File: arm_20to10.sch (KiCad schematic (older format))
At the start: 10 parts, among them J1 ARM_20PIN, J2 ARM_10PIN, SW1 DUAL_SWITCH_INV, U1 AAT3221 or LP5907

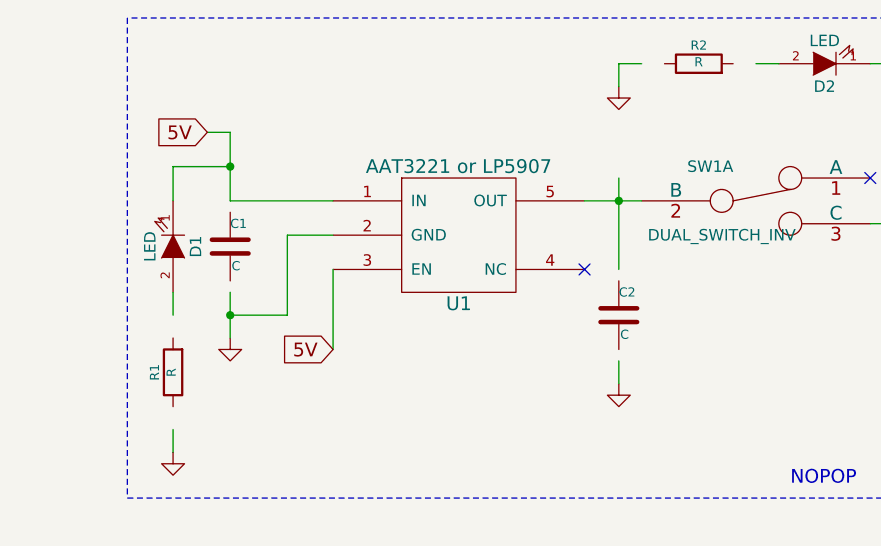
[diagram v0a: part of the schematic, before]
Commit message: - set some comp values
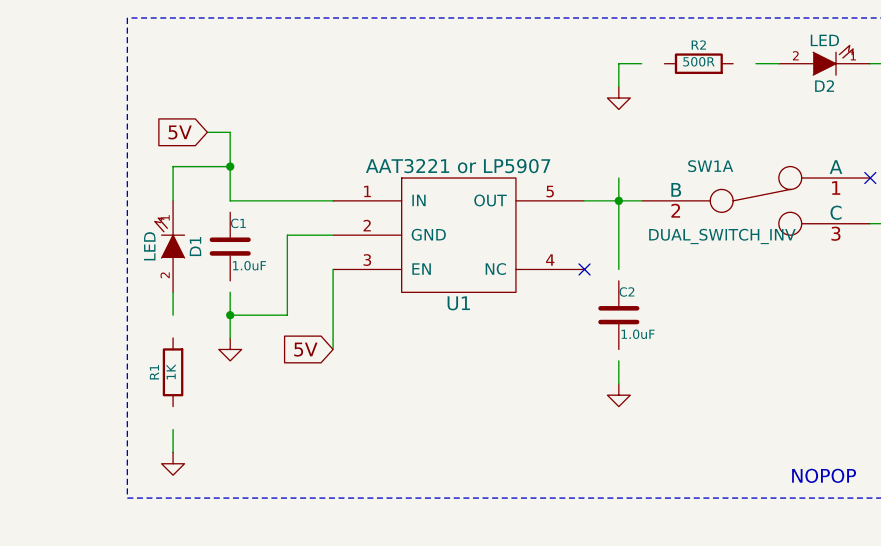
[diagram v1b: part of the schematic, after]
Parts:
- C1, C2: value C -> 1.0uF
- R1: value R -> 1K
- R2: value R -> 500R
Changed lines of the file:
@@
 P 8550 2200
 F 0 "C2" H 8550 2300 40  0000 L CNN
-F 1 "C" H 8556 2115 40  0000 L CNN
+F 1 "1.0uF" H 8556 2115 40  0000 L CNN
 F 2 "~" H 8588 2050 30  0000 C CNN
 F 3 "~" H 8550 2200 60  0000 C CNN
@@
 $EndComp
 NoConn ~ 8400 2000
-$Comp
-L C C1
-U 1 1 52FC308F
-P 6850 1900
-F 0 "C1" H 6850 2000 40  0000 L CNN
-F 1 "C" H 6856 1815 40  0000 L CNN
-F 2 "~" H 6888 1750 30  0000 C CNN
-F 3 "~" H 6850 1900 60  0000 C CNN
-	1    6850 1900
-	1    0    0    -1
-$EndComp
 Text GLabel 6750 1400 0    60   Input ~ 0
 5V
@@
 P 8900 1100
 F 0 "R2" V 8980 1100 40  0000 C CNN
-F 1 "R" V 8907 1101 40  0000 C CNN
+F 1 "500R" V 8907 1101 40  0000 C CNN
 F 2 "~" V 8830 1100 30  0000 C CNN
 F 3 "~" H 8900 1100 30  0000 C CNN
@@
 P 6600 2450
 F 0 "R1" V 6680 2450 40  0000 C CNN
-F 1 "R" V 6607 2451 40  0000 C CNN
+F 1 "1K" V 6607 2451 40  0000 C CNN
 F 2 "~" V 6530 2450 30  0000 C CNN
 F 3 "~" H 6600 2450 30  0000 C CNN
@@
 	9850 1100 9850 1800
 Connection ~ 9850 1800
+$Comp
+L C C1
+U 1 1 531B43FC
+P 6850 1900
+F 0 "C1" H 6850 2000 40  0000 L CNN
+F 1 "1.0uF" H 6856 1815 40  0000 L CNN
+F 2 "~" H 6888 1750 30  0000 C CNN
+F 3 "~" H 6850 1900 60  0000 C CNN
+	1    6850 1900
+	1    0    0    -1
+$EndComp
 $EndSCHEMATC

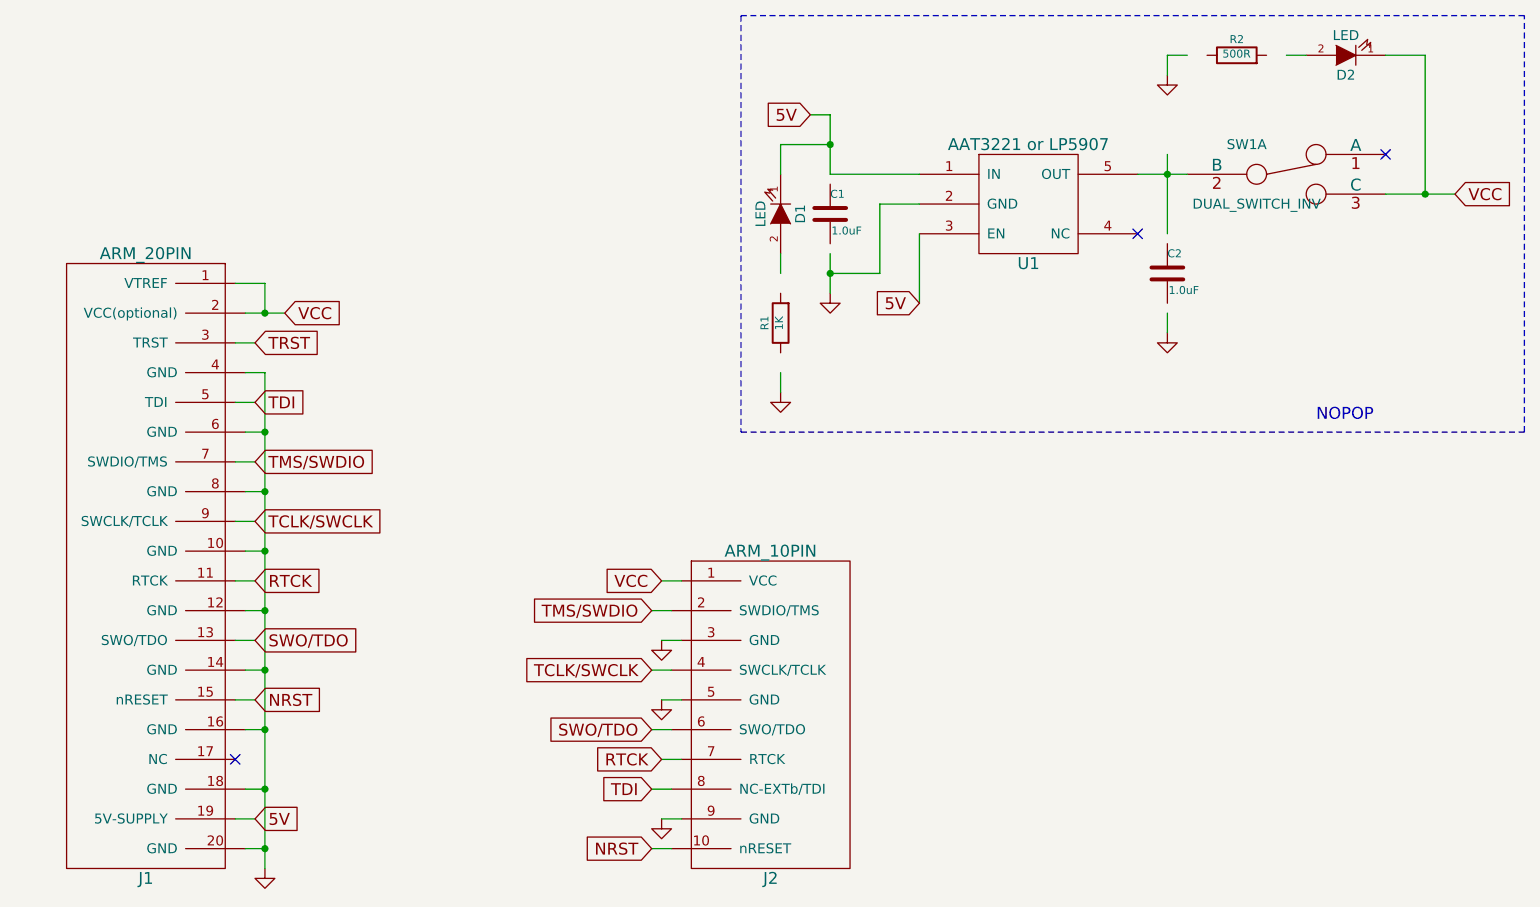
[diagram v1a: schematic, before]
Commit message: - redo with 0402 resistors
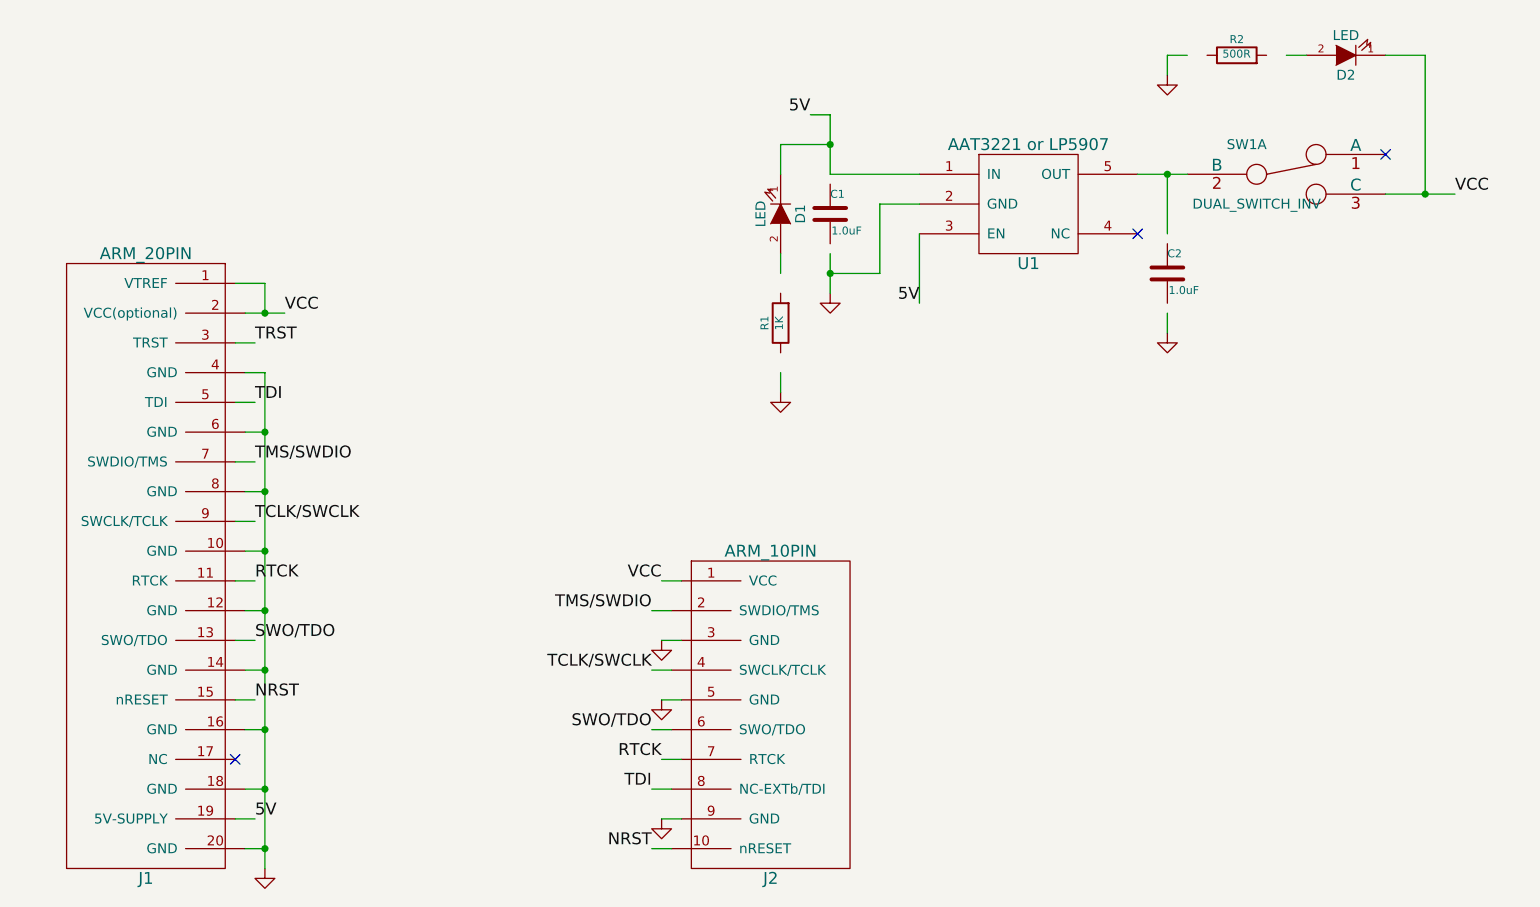
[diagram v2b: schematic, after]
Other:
- note removed: "NOPOP"
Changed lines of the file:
@@
 Sheet 1 1
 Title ""
-Date "8 mar 2014"
+Date "23 apr 2014"
 Rev ""
 Comp ""
@@
 	1    0    0    -1
 $EndComp
-Text GLabel 3950 3150 2    60   Input ~ 0
-TMS/SWDIO
-Text GLabel 3950 4050 2    60   Input ~ 0
-SWO/TDO
-Text GLabel 3950 4350 2    60   Input ~ 0
-NRST
 Wire Wire Line
 	3950 3150 3850 3150
@@
 Wire Wire Line
 	3950 4350 3850 4350
-Text GLabel 3950 2850 2    60   Input ~ 0
-TDI
 Wire Wire Line
 	3950 2850 3850 2850
-Text GLabel 3950 2550 2    60   Input ~ 0
-TRST
 Wire Wire Line
 	3950 2550 3850 2550
@@
 Wire Wire Line
 	6000 4650 6100 4650
-Text GLabel 5950 5100 0    60   Input ~ 0
-NRST
 Wire Wire Line
 	5950 5100 6050 5100
@@
 Wire Wire Line
 	6100 4050 6000 4050
-Text GLabel 5950 3900 0    60   Input ~ 0
-TMS/SWDIO
 Wire Wire Line
 	5950 3900 6050 3900
 Wire Wire Line
 	5950 4200 6050 4200
-Text GLabel 5950 4500 0    60   Input ~ 0
-SWO/TDO
 Wire Wire Line
 	6050 4500 5950 4500
-Text GLabel 5950 4800 0    60   Input ~ 0
-TDI
 Wire Wire Line
 	5950 4800 6050 4800
-Text GLabel 3950 4950 2    60   Input ~ 0
-5V
 Wire Wire Line
 	3950 4950 3850 4950
-Text GLabel 6000 3750 0    60   Input ~ 0
-VCC
 Wire Wire Line
 	6100 3750 6000 3750
-Text GLabel 4100 2400 2    60   Input ~ 0
-VCC
 Wire Wire Line
 	3900 2400 4100 2400
@@
 Connection ~ 4000 2400
 NoConn ~ 3850 4650
-Text GLabel 3950 3750 2    60   Input ~ 0
-RTCK
-Text GLabel 6000 4650 0    60   Input ~ 0
-RTCK
 $Comp
 L GND #PWR03
@@
 	1    0    0    -1
 $EndComp
-Text GLabel 3950 3450 2    60   Input ~ 0
-TCLK/SWCLK
-Text GLabel 5950 4200 0    60   Input ~ 0
-TCLK/SWCLK
 $Comp
 L GND #PWR04
@@
 $EndComp
 NoConn ~ 8400 2000
-Text GLabel 6750 1400 0    60   Input ~ 0
-5V
 Wire Wire Line
 	6750 1400 6850 1400
@@
 	7100 2200 6850 2200
 Connection ~ 6850 2200
-Text GLabel 7300 2350 0    60   Input ~ 0
-5V
 Wire Wire Line
 	7300 2000 7300 2350
@@
 Wire Wire Line
 	8550 2500 8550 2400
-Text GLabel 10000 1800 2    60   Input ~ 0
-VCC
 $Comp
 L DUAL_SWITCH_INV SW1
@@
 Wire Wire Line
 	8650 1700 8400 1700
-Text Notes 9300 2950 0    60   ~ 0
-NOPOP
 Wire Wire Line
 	10000 1800 9650 1800
-Wire Wire Line
-	8550 1600 8550 2000
 Connection ~ 8550 1700
 $Comp
@@
 Wire Wire Line
 	9250 1100 9150 1100
-Wire Notes Line
-	10350 900  6400 900
 $Comp
 L LED D1
@@
 	1    0    0    -1
 $EndComp
-Wire Notes Line
-	6400 3000 10350 3000
-Wire Notes Line
-	10350 3000 10350 900
-Wire Notes Line
-	6400 900  6400 3000
 Wire Wire Line
 	6600 2700 6600 2800
@@
 	1    0    0    -1
 $EndComp
+Wire Wire Line
+	8550 2000 8550 1700
+Text Label 4100 2400 0    60   ~ 0
+VCC
+Text Label 6000 3750 2    60   ~ 0
+VCC
+Text Label 10000 1800 0    60   ~ 0
+VCC
+Text Label 3950 2550 0    60   ~ 0
+TRST
+Text Label 3950 2850 0    60   ~ 0
+TDI
+Text Label 3950 3150 0    60   ~ 0
+TMS/SWDIO
+Text Label 3950 3450 0    60   ~ 0
+TCLK/SWCLK
+Text Label 3950 3750 0    60   ~ 0
+RTCK
+Text Label 3950 4050 0    60   ~ 0
+SWO/TDO
+Text Label 3950 4350 0    60   ~ 0
+NRST
+Text Label 3950 4950 0    60   ~ 0
+5V
+Text Label 6750 1400 2    60   ~ 0
+5V
+Text Label 7300 2350 2    60   ~ 0
+5V
+Text Label 5950 3900 2    60   ~ 0
+TMS/SWDIO
+Text Label 5950 4200 2    60   ~ 0
+TCLK/SWCLK
+Text Label 5950 4500 2    60   ~ 0
+SWO/TDO
+Text Label 6000 4650 2    60   ~ 0
+RTCK
+Text Label 5950 4800 2    60   ~ 0
+TDI
+Text Label 5950 5100 2    60   ~ 0
+NRST
 $EndSCHEMATC

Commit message: - start reworking board with new 20 pin header
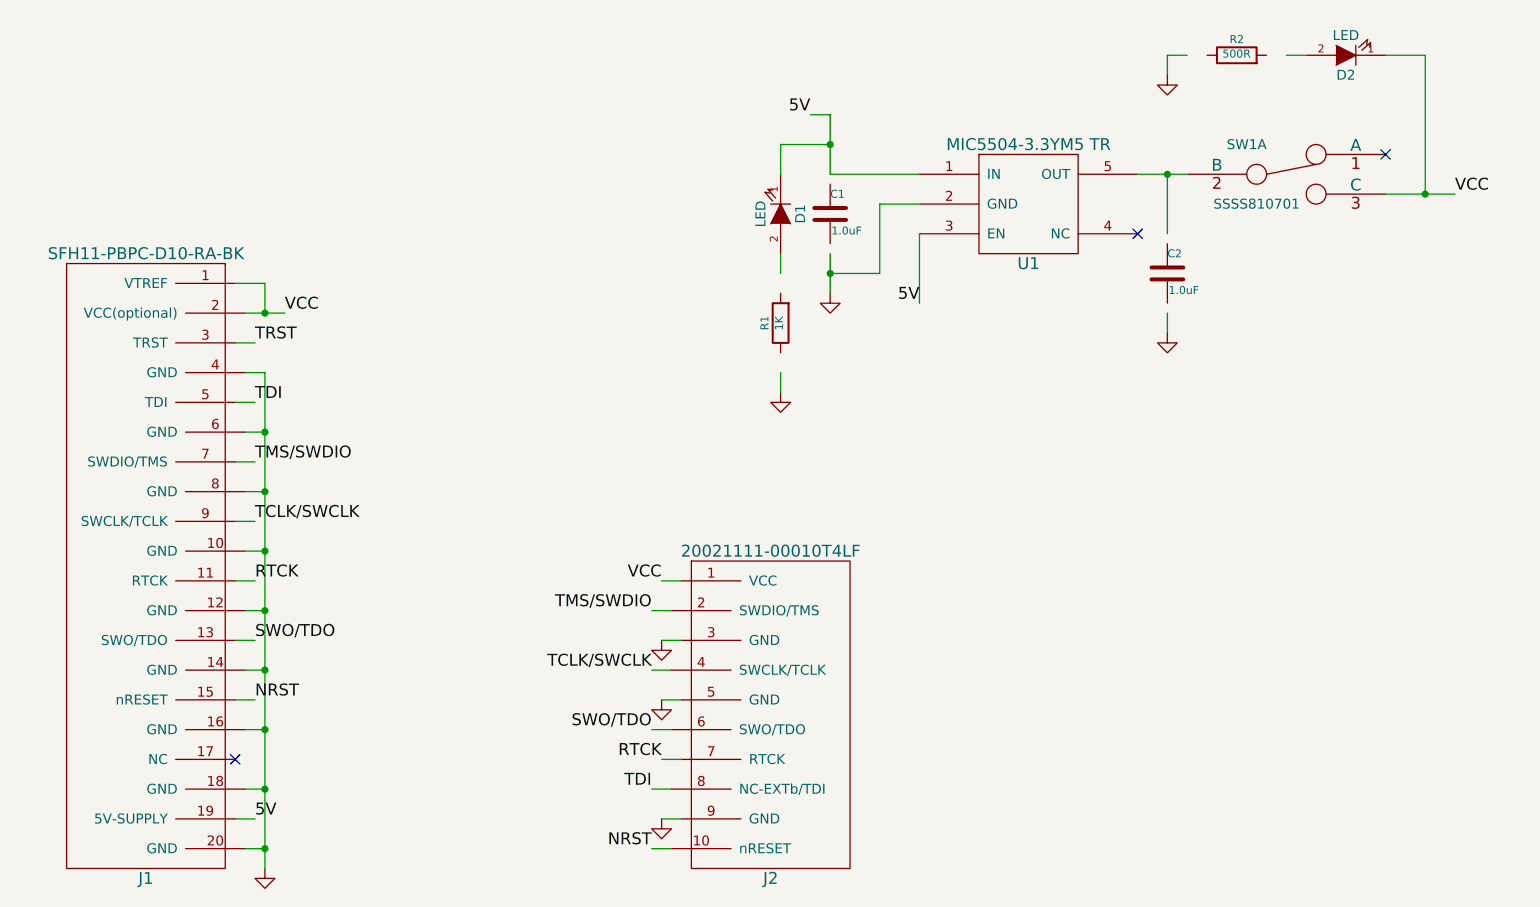
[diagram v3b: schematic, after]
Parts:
- J1: value ARM_20PIN -> SFH11-PBPC-D10-RA-BK
- J2: value ARM_10PIN -> 20021111-00010T4LF
- SW1: value DUAL_SWITCH_INV -> SSSS810701
- U1: value AAT3221 or LP5907 -> MIC5504-3.3YM5 TR
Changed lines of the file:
@@
 Sheet 1 1
 Title ""
-Date "23 apr 2014"
+Date "27 oct 2014"
 Rev ""
 Comp ""
@@
 P 6550 4250
 F 0 "J2" H 6550 3250 60  0000 C CNN
-F 1 "ARM_10PIN" H 6550 4900 60  0000 C CNN
+F 1 "20021111-00010T4LF" H 6550 4900 60  0000 C CNN
 F 2 "~" H 6550 4250 60  0000 C CNN
 F 3 "~" H 6550 4250 60  0000 C CNN
@@
 P 3400 3500
 F 0 "J1" H 3400 1750 60  0000 C CNN
-F 1 "ARM_20PIN" H 3400 4900 60  0000 C CNN
+F 1 "SFH11-PBPC-D10-RA-BK" H 3400 4900 60  0000 C CNN
 F 2 "~" H 3400 3500 60  0000 C CNN
 F 3 "~" H 3400 3500 60  0000 C CNN
@@
 P 7850 1950
 F 0 "U1" H 7850 1750 60  0000 C CNN
-F 1 "AAT3221 or LP5907" H 7850 2350 60  0000 C CNN
+F 1 "MIC5504-3.3YM5 TR" H 7850 2350 60  0000 C CNN
 F 2 "" H 7850 1950 60  0000 C CNN
 F 3 "" H 7850 1950 60  0000 C CNN
@@
 P 9150 1700
 F 0 "SW1" H 8950 1850 50  0000 C CNN
-F 1 "DUAL_SWITCH_INV" H 9000 1550 50  0000 C CNN
+F 1 "SSSS810701" H 9000 1550 50  0000 C CNN
 F 2 "~" H 9150 1700 60  0000 C CNN
 F 3 "~" H 9150 1700 60  0000 C CNN

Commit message: - pcb done.
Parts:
- C1, C2: footprint ~ -> SMD_Packages:SMD-0603_c
- D1, D2: footprint ~ -> SMD_Packages:SMD-0603
- J1: footprint ~ -> kicadlib:ARM_20_PIN_TH_RIGHTANGLE
- J2: footprint ~ -> kicadlib:ARM_10_PIN
- R1, R2: footprint ~ -> SMD_Packages:SMD-0603_r
- SW1: footprint ~ -> kicadlib:SWITCH_SLIDE_SSSS810701
- U1: footprint (none) -> kicadlib:sot23-5_noah
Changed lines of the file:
@@
 LIBS:kicadlib
 LIBS:arm_20to10-cache
-EELAYER 27 0
+EELAYER 25 0
 EELAYER END
 $Descr A4 11693 8268
@@
 F 0 "J2" H 6550 3250 60  0000 C CNN
 F 1 "20021111-00010T4LF" H 6550 4900 60  0000 C CNN
-F 2 "~" H 6550 4250 60  0000 C CNN
+F 2 "kicadlib:ARM_10_PIN" H 6550 4250 60  0001 C CNN
 F 3 "~" H 6550 4250 60  0000 C CNN
 	1    6550 4250
@@
 F 0 "J1" H 3400 1750 60  0000 C CNN
 F 1 "SFH11-PBPC-D10-RA-BK" H 3400 4900 60  0000 C CNN
-F 2 "~" H 3400 3500 60  0000 C CNN
+F 2 "kicadlib:ARM_20_PIN_TH_RIGHTANGLE" H 3400 3500 60  0001 C CNN
 F 3 "~" H 3400 3500 60  0000 C CNN
 	1    3400 3500
@@
 F 0 "U1" H 7850 1750 60  0000 C CNN
 F 1 "MIC5504-3.3YM5 TR" H 7850 2350 60  0000 C CNN
-F 2 "" H 7850 1950 60  0000 C CNN
+F 2 "kicadlib:sot23-5_noah" H 7850 1950 60  0001 C CNN
 F 3 "" H 7850 1950 60  0000 C CNN
 	1    7850 1950
@@
 F 0 "C2" H 8550 2300 40  0000 L CNN
 F 1 "1.0uF" H 8556 2115 40  0000 L CNN
-F 2 "~" H 8588 2050 30  0000 C CNN
+F 2 "SMD_Packages:SMD-0603_c" H 8588 2050 30  0001 C CNN
 F 3 "~" H 8550 2200 60  0000 C CNN
 	1    8550 2200
@@
 F 0 "SW1" H 8950 1850 50  0000 C CNN
 F 1 "SSSS810701" H 9000 1550 50  0000 C CNN
-F 2 "~" H 9150 1700 60  0000 C CNN
+F 2 "kicadlib:SWITCH_SLIDE_SSSS810701" H 9150 1700 60  0001 C CNN
 F 3 "~" H 9150 1700 60  0000 C CNN
 	1    9150 1700
@@
 F 0 "D2" H 9450 1200 50  0000 C CNN
 F 1 "LED" H 9450 1000 50  0000 C CNN
-F 2 "~" H 9450 1100 60  0000 C CNN
+F 2 "SMD_Packages:SMD-0603" H 9450 1100 60  0001 C CNN
 F 3 "~" H 9450 1100 60  0000 C CNN
 	1    9450 1100
@@
 F 0 "R2" V 8980 1100 40  0000 C CNN
 F 1 "500R" V 8907 1101 40  0000 C CNN
-F 2 "~" V 8830 1100 30  0000 C CNN
+F 2 "SMD_Packages:SMD-0603_r" V 8830 1100 30  0001 C CNN
 F 3 "~" H 8900 1100 30  0000 C CNN
 	1    8900 1100
@@
 F 0 "D1" H 6600 2000 50  0000 C CNN
 F 1 "LED" H 6600 1800 50  0000 C CNN
-F 2 "~" H 6600 1900 60  0000 C CNN
+F 2 "SMD_Packages:SMD-0603" H 6600 1900 60  0001 C CNN
 F 3 "~" H 6600 1900 60  0000 C CNN
 	1    6600 1900
@@
 F 0 "R1" V 6680 2450 40  0000 C CNN
 F 1 "1K" V 6607 2451 40  0000 C CNN
-F 2 "~" V 6530 2450 30  0000 C CNN
+F 2 "SMD_Packages:SMD-0603_r" V 6530 2450 30  0001 C CNN
 F 3 "~" H 6600 2450 30  0000 C CNN
 	1    6600 2450
@@
 F 0 "C1" H 6850 2000 40  0000 L CNN
 F 1 "1.0uF" H 6856 1815 40  0000 L CNN
-F 2 "~" H 6888 1750 30  0000 C CNN
+F 2 "SMD_Packages:SMD-0603_c" H 6888 1750 30  0001 C CNN
 F 3 "~" H 6850 1900 60  0000 C CNN
 	1    6850 1900
